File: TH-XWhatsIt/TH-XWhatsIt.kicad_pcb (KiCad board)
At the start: 2 copper layers, 178 x 115.5 mm, 39 parts, among them J1 COLUMNS, J10 DISPLAYWRITER PLUGBOARD CONNE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, J11 DISPLAYWRITER PLUGBOARD ROWS, J12 EXPANSION HEADER, J2 ROWS, J3 MODEL F PLUGBOARD COLUMNS, J4 MODEL F PLUGBOARD CONNECTOR, J5 MODEL F PLUGBOARD ROWS, J6 BEAMSPRING PLUGBOARD COLUMNS, J7 BEAMSPRING PLUGBOARD CONNECTOR, J8 BEAMSPRING PLUGBOARD ROWS, J9 DISPLAYWRITER PLUGBOARD COLUM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, U1 LM339, U2 MCP4921-EP, U3 74HCT595, U5 74HCT595, U6 LM339, U7 ProMicro, U8 74HCT595

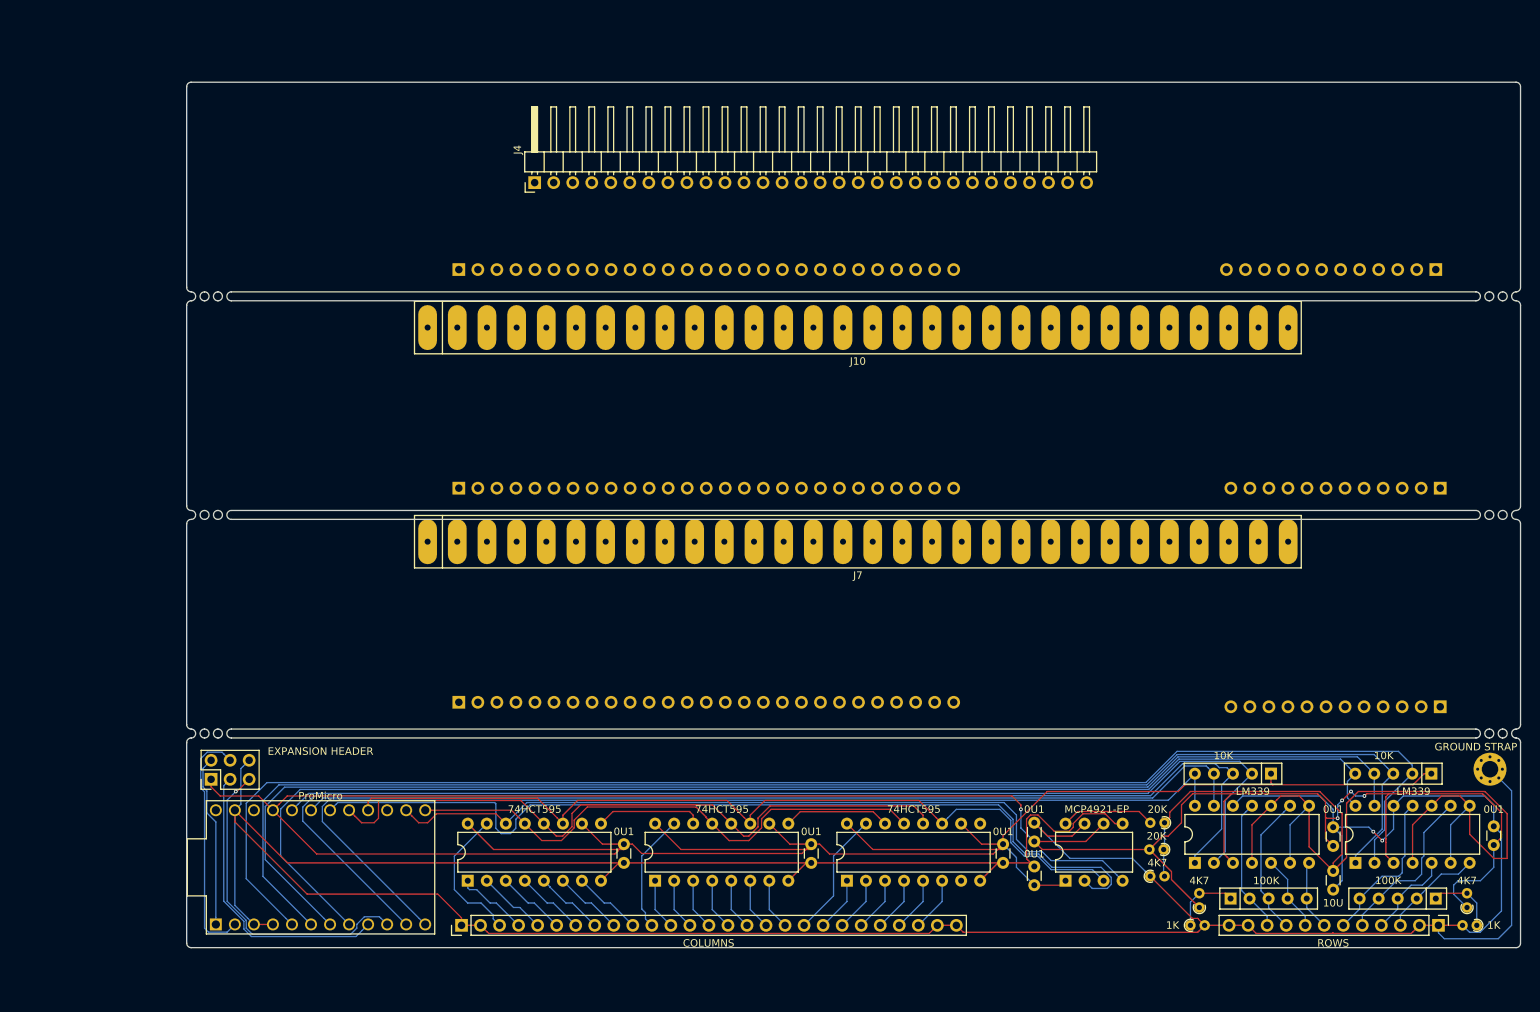
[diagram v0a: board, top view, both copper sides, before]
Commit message: version bump to 2.0 due to header position changes finished wiring up most of the plugboards, but displaywriter as per usual is the most annoying.....see changes file for more details (jan 3rd, 2020)
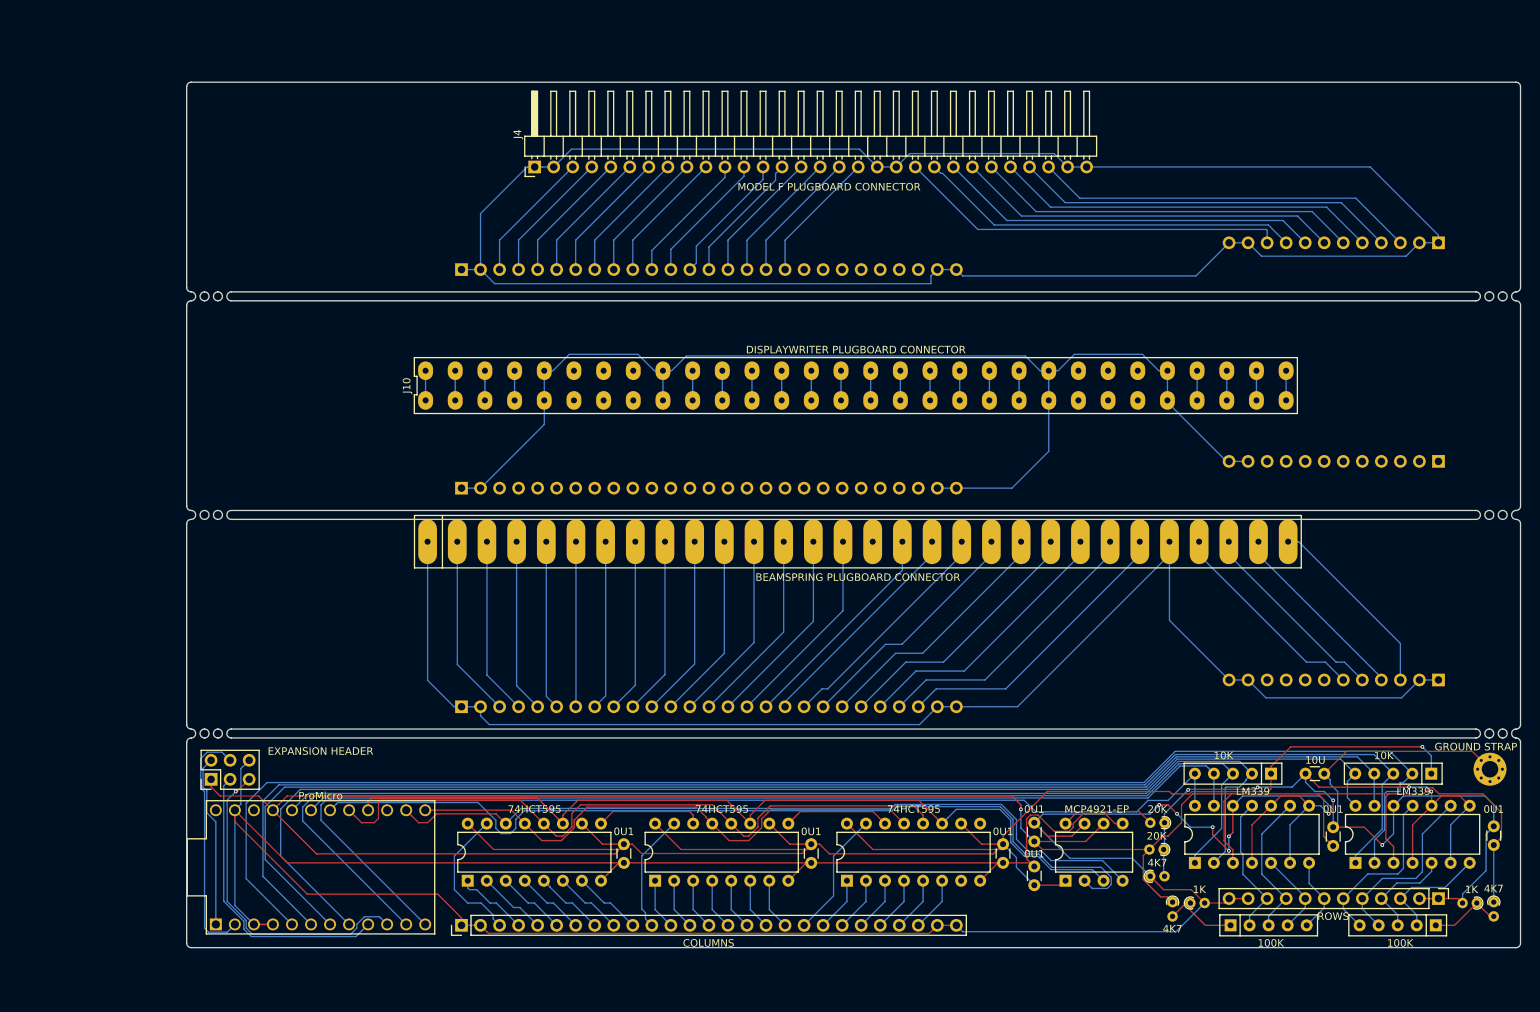
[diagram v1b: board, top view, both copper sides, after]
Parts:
- J10: footprint TH-XWhatsIt:3..6mm_cardedge -> TH-XWhatsIt:DIP-60_155_ELL
- moved C2 15.5 mm to (205.4, 125.6), turned to 180 degrees
- moved J10 7.74 mm to (142.9, 73.8)
- moved R1 3.64 mm to (228.0, 142.8), turned to 270 degrees
- moved R6 3.64 mm to (185.1, 142.8), turned to 270 degrees
- moved J5 3.59 mm to (220.6, 54.8)
- moved J11 3.58 mm to (220.6, 83.9)
- moved J8 3.58 mm to (220.6, 113.1)
- moved J2 3.57 mm to (220.6, 142.3)
- moved RN1 3.57 mm to (220.3, 145.9)
- moved RN3 3.57 mm to (192.9, 145.9)
- moved R2 2.98 mm to (225.7, 142.9)
- moved R7 2.98 mm to (187.5, 142.9)
- moved J4 2.09 mm to (100.0, 44.6)
- moved J6 0.69 mm to (90.2, 116.7)
- moved J3 0.36 mm to (90.2, 58.3)
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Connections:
- J11 pad 10: /displaywriter plugboard/DWSENSE8 -> /displaywriter plugboard/DWSENSE5
- J11 pad 7: /displaywriter plugboard/DWSENSE5 -> /displaywriter plugboard/DWSENSE8
- J11 pad 8: /displaywriter plugboard/DWSENSE6 -> /displaywriter plugboard/DWSENSE7
- J11 pad 9: /displaywriter plugboard/DWSENSE7 -> /displaywriter plugboard/DWSENSE6
- J2 pad 8: SENSE6 -> SENSE7
- J2 pad 9: SENSE7 -> SENSE6
- J5 pad 10: /model f plugboard/MFSENSE8 -> /model f plugboard/MFSENSE1
- J5 pad 3: /model f plugboard/MFSENSE1 -> /model f plugboard/MFSENSE8
- J5 pad 4: /model f plugboard/MFSENSE2 -> /model f plugboard/MFSENSE7
- J5 pad 5: /model f plugboard/MFSENSE3 -> /model f plugboard/MFSENSE6
- J5 pad 6: /model f plugboard/MFSENSE4 -> /model f plugboard/MFSENSE5
- J5 pad 7: /model f plugboard/MFSENSE5 -> /model f plugboard/MFSENSE4
- J5 pad 8: /model f plugboard/MFSENSE6 -> /model f plugboard/MFSENSE3
- J5 pad 9: /model f plugboard/MFSENSE7 -> /model f plugboard/MFSENSE2
- J8 pad 3: /beamspring plugboard/BSSENSE1 -> /beamspring plugboard/BSSENSE4
- J8 pad 4: /beamspring plugboard/BSSENSE2 -> /beamspring plugboard/BSSENSE3
- J8 pad 5: /beamspring plugboard/BSSENSE3 -> /beamspring plugboard/BSSENSE2
- J8 pad 6: /beamspring plugboard/BSSENSE4 -> /beamspring plugboard/BSSENSE1
- RN3 pad 3: SENSE7 -> SENSE6
- RN3 pad 4: SENSE6 -> SENSE7
- RN4 pad 2: ROW6 -> ROW7
- RN4 pad 5: ROW7 -> ROW6
- U6 pad 14: ROW7 -> ROW6
- U6 pad 2: ROW6 -> ROW7
- U6 pad 5: SENSE6 -> SENSE7
- U6 pad 9: SENSE7 -> SENSE6
- U7 pad 12: ROW7 -> ROW6
- U7 pad 20: ROW6 -> ROW7
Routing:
- net /model f plugboard/MFGROUND: track 0.00 -> 282.3 mm
- net /beamspring plugboard/BSGROUND: track 0.00 -> 183.5 mm
- net /displaywriter plugboard/DWGROUND: track 0.00 -> 160.0 mm
- net /model f plugboard/MFSENSE1: track 0.00 -> 52.1 mm
- net /model f plugboard/MFSENSE8: track 0.00 -> 51.1 mm
- net /model f plugboard/MFSENSE6: track 0.00 -> 51.1 mm
- net /model f plugboard/MFSENSE3: track 0.00 -> 51.1 mm
- net /model f plugboard/MFSENSE7: track 0.00 -> 51.1 mm
- net /model f plugboard/MFSENSE5: track 0.00 -> 51.1 mm
- net /model f plugboard/MFSENSE4: track 0.00 -> 51.1 mm
- net /model f plugboard/MFSENSE2: track 0.00 -> 51.1 mm
- net SETPOINT: track 148.6 -> 107.1 mm, vias 0 -> 6
- net /beamspring plugboard/BSCOL23: track 0.00 -> 39.7 mm
- net /beamspring plugboard/BSCOL22: track 0.00 -> 38.3 mm
- net /beamspring plugboard/BSCOL21: track 0.00 -> 36.9 mm
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
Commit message: finished wiring the dispalywriter plugboard, and added grounding straps to plugboards
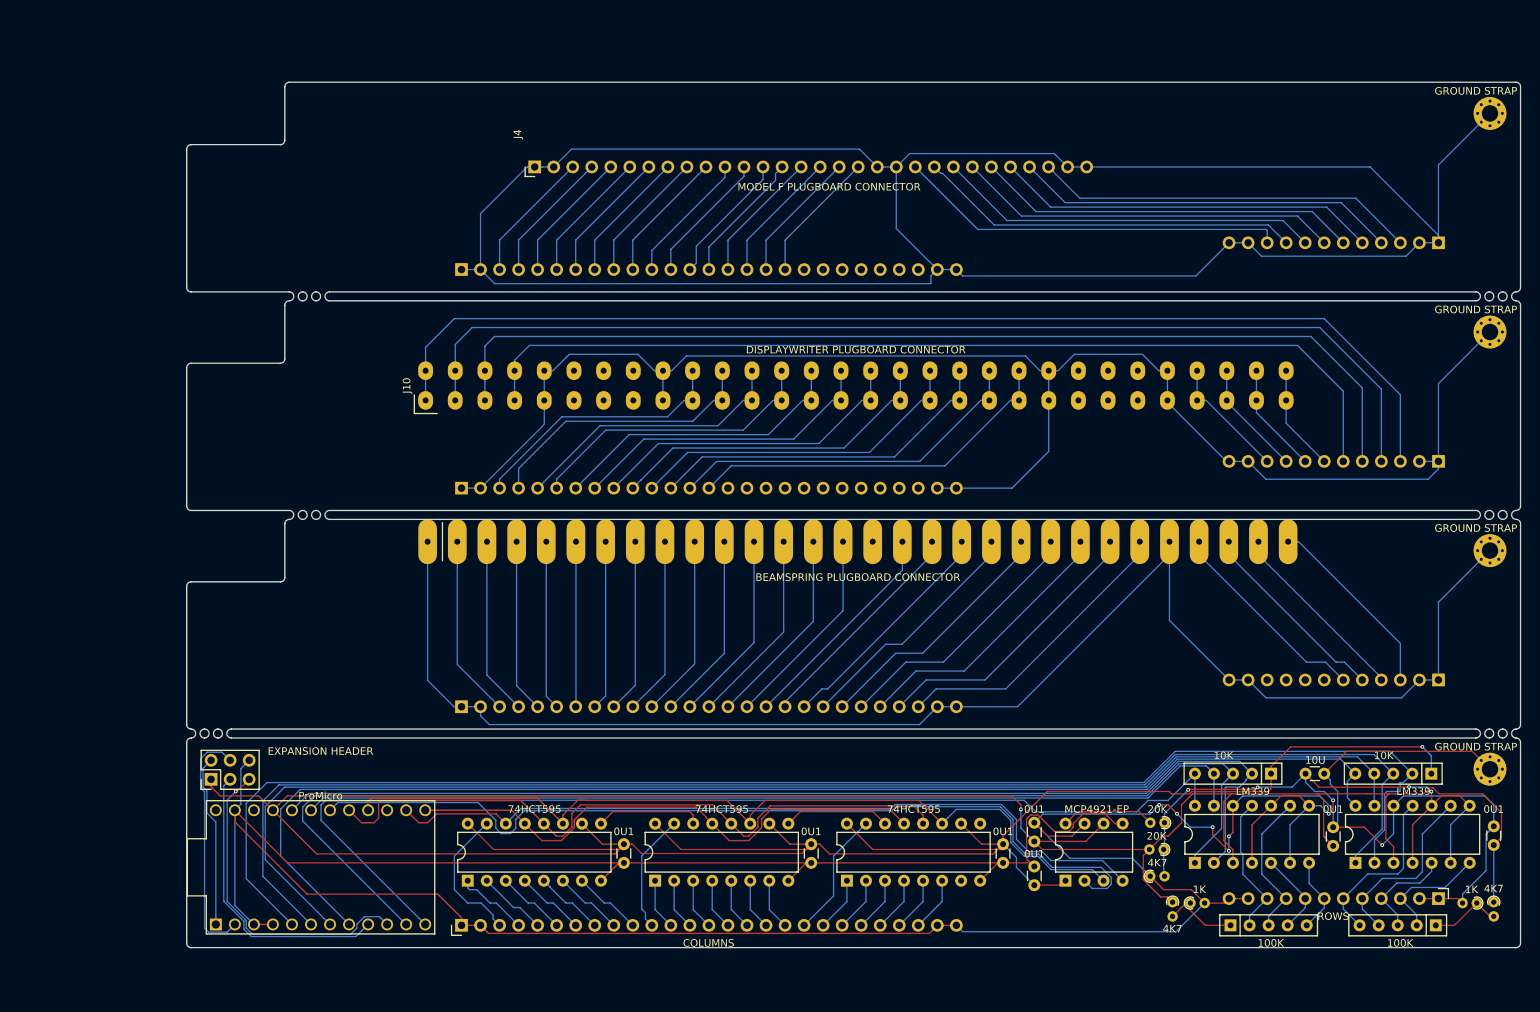
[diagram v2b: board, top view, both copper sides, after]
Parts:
- added H2: GROUND STRAP, MountingHole:MountingHole_2.2mm_M2_Pad_Via, F.Cu at (227.5, 37.5)
- added H3: GROUND STRAP, MountingHole:MountingHole_2.2mm_M2_Pad_Via, F.Cu at (227.5, 95.8)
- added H4: GROUND STRAP, MountingHole:MountingHole_2.2mm_M2_Pad_Via, F.Cu at (227.5, 66.7)
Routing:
- net /displaywriter plugboard/DWSENSE1: track 3.96 -> 151.8 mm
- net /displaywriter plugboard/DWSENSE2: track 3.96 -> 145.0 mm
- net /displaywriter plugboard/DWSENSE3: track 3.96 -> 137.5 mm
- net /displaywriter plugboard/DWSENSE4: track 3.96 -> 128.7 mm
- net /displaywriter plugboard/DWGROUND: track 160.0 -> 210.6 mm
- net /displaywriter plugboard/DWCOL12: track 3.96 -> 50.2 mm
- net /displaywriter plugboard/DWCOL11: track 3.96 -> 48.8 mm
- net /displaywriter plugboard/DWCOL10: track 3.96 -> 47.4 mm
- net /displaywriter plugboard/DWCOL9: track 3.96 -> 45.9 mm
- net /displaywriter plugboard/DWCOL8: track 3.96 -> 44.5 mm
- net /displaywriter plugboard/DWCOL7: track 3.96 -> 43.1 mm
- net /displaywriter plugboard/DWCOL6: track 3.96 -> 41.7 mm
- net /displaywriter plugboard/DWCOL5: track 3.96 -> 40.3 mm
- net /model f plugboard/MFGROUND: track 282.3 -> 318.4 mm
- net /displaywriter plugboard/DWCOL4: track 3.96 -> 39.5 mm
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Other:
- outline, holes or cut-outs redrawn

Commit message: rumors of my demise are greatly exaggerated, updates; more incoming now powered with new pc! thanks for being patient, please inform of futher changes!
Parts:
- removed C2: 10U, Capacitor_THT:C_Disc_D3.0mm_W1.6mm_P2.50mm
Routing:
- net GNDA: track 487.0 -> 455.3 mm
- net SETPOINT: track 107.1 -> 97.4 mm
- net +5VA: track 517.5 -> 516.9 mm
